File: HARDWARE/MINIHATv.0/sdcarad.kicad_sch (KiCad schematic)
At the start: 28 parts, among them J2 Micro_SD_Card_Det2, J5 Micro_SD_Card_Det2

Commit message: buses defined ind project settings, added stm antenna footprint, organized TOP
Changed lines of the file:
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@@
 		)
 	)
-	(hierarchical_label "SDIO{DAT0 DAT1 DAT2 DAT3 CMD CLK}"
+	(hierarchical_label "SDIO"
 		(shape input)
 		(at 53.34 60.96 180)

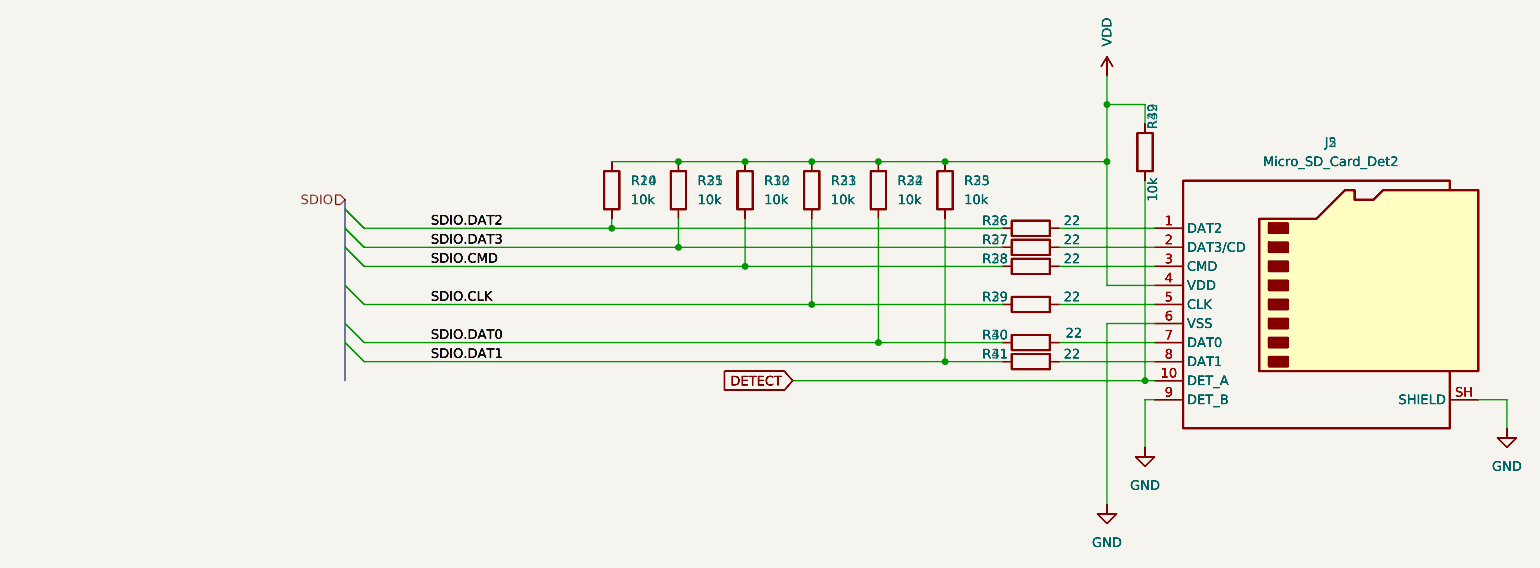
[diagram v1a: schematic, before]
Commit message: added i2c for hdmi
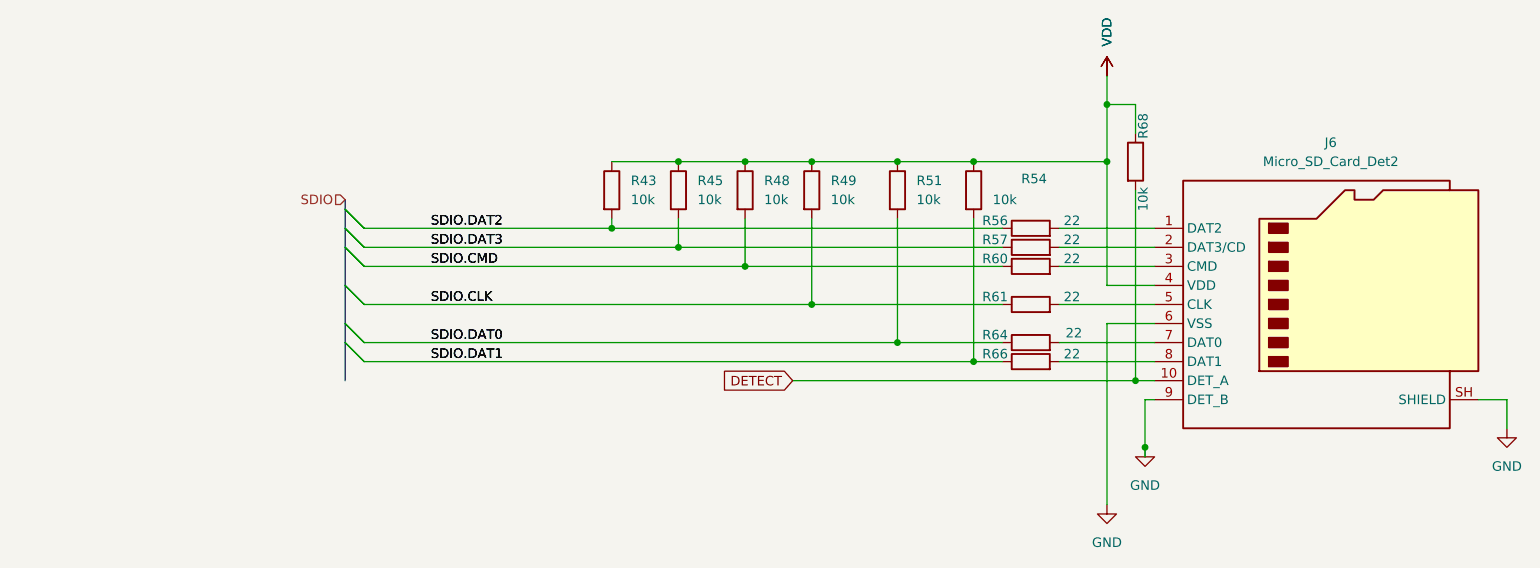
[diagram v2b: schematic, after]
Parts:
- removed J5: Micro_SD_Card_Det2, Connector_Card:microSD_HC_Hirose_DM3AT-SF-PEJM5, symbol Connector:Micro_SD_Card_Det2
- removed R10 (x2), R22, R23, R25, R33, R39: 10k, symbol Device:R
- removed R27, R30, R31, R36, R38, R39: 22, symbol Device:R
- renumbered J2 to J6, R24 to R43, R31 to R45, R32 to R48, R21 to R49, R34 to R51, R35 to R54, R26 to R56, R37 to R57, R28 to R60, R29 to R61, R40 to R64, R41 to R66, R42 to R68
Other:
- moved on the sheet: R51, R54, R68
